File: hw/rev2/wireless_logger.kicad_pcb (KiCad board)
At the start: 4 copper layers, 98 parts, among them J1 FCI 10118194, J3 SSD1306_SER, J4 SWD_10PIN, Q1 2N7002P, Q2 2N7002P, U1 MT29FXX01A, U10 CC2541, U11 STM32F40X_BGA176, U2 MAG3110, U3 MMA8452Q, U4 LPS331AP, U5 L3GD20, U6 MCP111T-315, U7 BQ24095, U8 TPS62698, U9 CC1101, X1 FA-128 26.0000MF10Z-W3, X2 9HT10-32.768KBZF-T, X3 FA-128 32.0000MF20X-K3, X4 XRCGB25M000F0L00R0, X5 9HT10-32.768KBZF-T

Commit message: Uhhhh, secondary interconnect assignment and a LOT of routing
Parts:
- added C10: 100n, SMD0603, F.Cu at (195.9, 111.4)
- added C11: 100n, SMD0603, F.Cu at (198.6, 112.4)
- added C12: 100n, SMD0603, F.Cu at (182.8, 121.7)
- added C13: 10n, SMD0402, B.Cu at (179.1, 118.9)
- added C14: 2.2u, SMD0603, F.Cu at (184.4, 128.5)
- added C15: 100n, SMD0603, B.Cu at (177.0, 125.7)
- added C16: 100p, SMD0402, B.Cu at (186.2, 122.8)
- added C17: 100n, SMD0603, B.Cu at (177.4, 117.8)
- added C18: 1u, SMD0603, B.Cu at (176.4, 119.8)
- added C19: 10n, SMD0402, F.Cu at (176.2, 123.6)
- added C20: 2.2u, SMD0603, B.Cu at (187.4, 155.9)
- added C21: 2.2u, SMD0603, F.Cu at (191.9, 153.6)
- added C22: 10u, SMD0805, B.Cu at (198.5, 157.3)
- added C27: 1u, SMD0603, F.Cu at (173.5, 142.9)
- added C28: 15p, SMD0402, F.Cu at (170.6, 139.0)
- added C29: 15p, SMD0402, F.Cu at (170.6, 137.1)
- added C3: 2.2u, SMD0603, F.Cu at (190.8, 111.2)
- added C30: 1n, SMD0402, F.Cu at (181.6, 136.6)
- added C31: 12p, SMD0402, F.Cu at (178.8, 134.6)
- added C32: 12p, SMD0402, F.Cu at (182.5, 134.1)
- added C4: 100n, SMD0603, F.Cu at (182.7, 120.5)
- added C5: 100n, SMD0603, F.Cu at (197.4, 113.3)
- added C6: 100p, SMD0402, F.Cu at (183.3, 128.4)
- added C61: 10n, SMD0402, B.Cu at (172.2, 114.4)
- added C62: 10n, SMD0402, B.Cu at (172.9, 120.6)
- added C63: 10n, SMD0402, B.Cu at (172.7, 126.8)
- added C64: 10n, SMD0402, B.Cu at (173.1, 148.7)
- added C7: 1u, SMD0603, F.Cu at (193.3, 115.0)
- added C8: 100n, SMD0603, F.Cu at (180.0, 131.5)
- added C9: 100n, SMD0603, F.Cu at (190.9, 113.2)
- added J2: CONN_2, HDR_2X1_50MIL, F.Cu at (193.9, 158.7)
- added J5: CONN_5, HDR_5X1_50MIL, F.Cu at (184.5, 152.7)
- added P1: CONN_6X2, HDR_6X2_50MIL, F.Cu at (192.3, 128.3)
- added R30: 470k, SMD0402, B.Cu at (173.0, 112.1)
- added R31: 470k, SMD0402, B.Cu at (172.9, 117.5)
- added R32: 470k, SMD0402, B.Cu at (171.8, 126.8)
- added R33: 470k, SMD0402, B.Cu at (173.0, 146.6)
- added R34: 10k, SMD0402, B.Cu at (190.2, 126.3)
- added R35: 10k, SMD0402, B.Cu at (190.2, 127.5)
- C1, C26, C34, C35, C48, C54, C58, R10, R14, R16, R17, R18, R20, R21, R22, R5, R8, U1: moved to B.Cu
- C38: moved to F.Cu
- moved R12 43.6 mm to (196.6, 158.5)
- moved R25 43.5 mm to (193.1, 111.2)
- moved R26 42.1 mm to (192.9, 113.1), turned to 90 degrees
- moved R9 40.8 mm to (196.7, 151.7)
- moved R10 39.0 mm to (192.3, 157.0)
- moved R8 38.4 mm to (192.1, 156.0)
- moved R27 37.5 mm to (195.5, 131.4), turned to 180 degrees
- moved R28 37.3 mm to (195.5, 132.6), turned to 180 degrees
- moved R21 36.6 mm to (181.1, 110.7), turned to 180 degrees
- moved R11 36.2 mm to (191.9, 151.4), turned to 45 degrees
- moved C26 36.1 mm to (173.9, 158.2), turned to 180 degrees
- moved R13 35.9 mm to (178.5, 151.4), turned to 180 degrees
- moved R22 30.2 mm to (188.7, 138.1)
- moved R4 29.9 mm to (181.9, 125.3), turned to 180 degrees
- moved C54 29.8 mm to (188.1, 140.3)
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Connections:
- net N-00000242 renamed /Bluetooth/BT_ANT_DN
- net N-00000243 renamed /Bluetooth/BT_ANT_DP
- net N-00000244 renamed /Bluetooth/BT_ANT_SE
- C1 pad 2: VDD -> V3
- C2 pad 2: VDD -> V3
- C38 pad 2: N-0000078 -> V3
- C45 pad 2: VDD -> V3
- C46 pad 2: VDD -> V3
- C47 pad 2: VDD -> V3
- C48 pad 2: VDD -> V3
- C49 pad 2: VDD -> V3
- C50 pad 2: VDD -> V3
- C51 pad 2: VDD -> V3
- C52 pad 2: VDD -> V3
- C53 pad 2: VDD -> V3
- C54 pad 2: VDD -> V3
- C55 pad 2: VDD -> V3
- C56 pad 2: VDD -> V3
- C57 pad 2: VDD -> V3
- C58 pad 2: VDD -> V3
- D1 pad 1: VDD -> V3
- J3 pad 10: (no net) -> /STM32F4/OLED_nD/C
- J3 pad 7: VDD -> V3
- J3 pad 8: (no net) -> /STM32F4/OLED_nCS
- J4 pad 1: N-0000078 -> V3
- PB1 pad 1: /STM32F4/EXTI5 -> N-0000047
- PB2 pad 1: /STM32F4/EXTI6 -> N-0000046
- PB3 pad 1: /STM32F4/EXTI7 -> N-0000045
- PB4 pad 1: /STM32F4/EXTI8 -> N-0000044
- R13 pad 1: VDD -> V3
- R15 pad 2: VDD -> V3
- R16 pad 1: /STM32F4/BT_NRESET -> /Bluetooth/RF_RESET_N_LOCAL
- R17 pad 1: /STM32F4/BT_NRESET -> /Bluetooth/RF_RESET_N_LOCAL
- R20 pad 1: GND -> /OLED/OLED_GND
- R23 pad 1: VDD -> V3
- R24 pad 1: VDD -> V3
- R25 pad 1: VDD -> V3
- R26 pad 1: VDD -> V3
- R27 pad 2: (no net) -> /STM32F4/LED1
- R28 pad 2: (no net) -> /STM32F4/LED2
- R29 pad 2: (no net) -> /STM32F4/LED3
- R5 pad 1: VDD -> V3
- R6 pad 2: VDD -> V3
- R7 pad 2: VDD -> V3
- U1 pad D3: VDD -> V3
- U1 pad G5: VDD -> V3
- U1 pad G6: VDD -> V3
- U1 pad J8: VDD -> V3
- U1 pad K7: (no net) -> /STM32F4/FLASH_nCS
- U10 pad 10: VDD -> V3
- U10 pad 13: (no net) -> /STM32F4/EXTI2
- U10 pad 20: /STM32F4/BT_NRESET -> /Bluetooth/RF_RESET_N_LOCAL
- U10 pad 21: VDD -> V3
- U10 pad 24: VDD -> V3
- U10 pad 27: VDD -> V3
- U10 pad 28: VDD -> V3
- U10 pad 29: VDD -> V3
- U10 pad 31: VDD -> V3
- U10 pad 39: VDD -> V3
- U10 pad GND: (no net) -> GND
- U11 pad A1: (no net) -> /STM32F4/LED2
- U11 pad A2: (no net) -> /STM32F4/LED3
- U11 pad A4: (no net) -> /Sensors/ACC_INT1
- U11 pad A6: (no net) -> /STM32F4/GYRO_nCS
- U11 pad B1: (no net) -> /OLED/EN
- U11 pad B11: (no net) -> /STM32F4/UART2_RX
- U11 pad B2: (no net) -> /STM32F4/LED1
- U11 pad B5: (no net) -> /STM32F4/FLASH_nCS
- U11 pad B7: (no net) -> /Sensors/PRS_SPI_nCS
- U11 pad C11: (no net) -> /STM32F4/UART2_TX
- U11 pad C5: VDD -> V3
- U11 pad C6: VDD -> V3
- U11 pad C7: VDD -> V3
- U11 pad C8: VDD -> V3
- U11 pad C9: VDD -> V3
- U11 pad D1: (no net) -> /STM32F4/OLED_nCS
- U11 pad D2: (no net) -> /STM32F4/OLED_nRES
- U11 pad F14: (no net) -> /STM32F4/I2C3_SDA
- U11 pad F15: (no net) -> /STM32F4/I2C3_SCL
- U11 pad F3: VDD -> V3
- U11 pad G13: VDD -> V3
- U11 pad G14: (no net) -> /STM32F4/REG_nUSB_CONN
- U11 pad G15: (no net) -> /STM32F4/REG_nCHG
- U11 pad G3: VDD -> V3
- U11 pad H13: VDD -> V3
- U11 pad H15: (no net) -> /Power/MODE
- U11 pad J12: VDD -> V3
- U11 pad J13: VDD -> V3
- U11 pad K1: (no net) -> /STM32F4/EXTI7
- U11 pad K4: VDD -> V3
- U11 pad M3: (no net) -> /STM32F4/EXTI1
- U11 pad M6: (no net) -> /STM32F4/EXTI2
- U11 pad N10: VDD -> V3
- U11 pad N8: VDD -> V3
- U11 pad N9: VDD -> V3
- U11 pad P1: VDD -> V3
- U11 pad P12: (no net) -> /STM32F4/SPI2_NSS
- U11 pad R1: VDD -> V3
- U11 pad R10: (no net) -> /STM32F4/BT_NRESET
- U11 pad R11: (no net) -> /STM32F4/CC1101_nCS
- U11 pad R15: (no net) -> /STM32F4/SPI2_MOSI
- U11 pad R2: (no net) -> /STM32F4/OLED_nD/C
- U11 pad R8: /STM32F4/EXTI7 -> (no net)
- U2 pad 2: VDD -> V3
- U2 pad 8: VDD -> V3
- U3 pad 1: VDD -> V3
- U3 pad 11: (no net) -> /Sensors/ACC_INT1
- U3 pad 14: VDD -> V3
- U4 pad 1: VDD -> V3
- U4 pad 14: VDD -> V3
- U5 pad 1: VDD -> V3
- U5 pad 15: VDD -> V3
- U5 pad 16: VDD -> V3
- U7 pad 5: (no net) -> /STM32F4/REG_nUSB_CONN
- U7 pad 8: (no net) -> /STM32F4/REG_nCHG
- U7 pad GND: (no net) -> GND
- U8 pad 3: (no net) -> GND
- U9 pad 11: VDD -> V3
- U9 pad 18: VDD -> V3
- U9 pad 4: VDD -> V3
- U9 pad 9: VDD -> V3
- X1 pad GND: (no net) -> GND
- X3 pad GND: (no net) -> GND
- X4 pad GND: (no net) -> GND
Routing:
- net V3: track 0.00 -> 273.7 mm, vias 0 -> 27
- net GND: track 46.1 -> 245.8 mm, vias 2 -> 45
- net Vbat: track 0.00 -> 92.0 mm, vias 0 -> 8
- net /Sensors/GYR_SPI_MOSI: track 0.00 -> 82.8 mm, vias 0 -> 8
- net /OLED/SDIN: track 0.00 -> 68.9 mm, vias 0 -> 5
- net /Sensors/ACC_I2C_SCL: track 0.00 -> 66.0 mm, vias 0 -> 3
- net /OLED/SCLK: track 0.00 -> 64.7 mm, vias 0 -> 3
- net /Sensors/GYR_SPI_MISO: track 0.00 -> 59.5 mm, vias 0 -> 5
- net /STM32F4/I2C3_SDA: track 0.00 -> 56.6 mm, vias 0 -> 4
- net /Sensors/GYR_SPI_CLK: track 0.00 -> 56.4 mm, vias 0 -> 6
- net /STM32F4/I2C3_SCL: track 0.00 -> 55.9 mm, vias 0 -> 4
- net /Sensors/ACC_I2C_SDA: track 0.00 -> 53.2 mm, vias 0 -> 3
- net Vbus: track 0.00 -> 50.8 mm, vias 0 -> 2
- net /STM32F4/SPI2_CLK: track 0.00 -> 49.3 mm, vias 0 -> 3
- net /STM32F4/SPI2_NSS: track 0.00 -> 48.6 mm, vias 0 -> 3
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- added copper zone on GND_PLANE, net /OLED/OLED_GND
- added copper zone on B.Cu, net GND
- added copper zone on GND_PLANE, net GND
- added copper zone on Inner2.Cu, net V3
- removed copper zone on GND, net /OLED/OLED_GND
- removed copper zone on GND, net GND
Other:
- net class 50OHM added: clearance 0.1524, trace_width 0.2032, via_dia 0.635, via_drill 0.3048
- net class Default: trace_width 0.2032 -> 0.1524

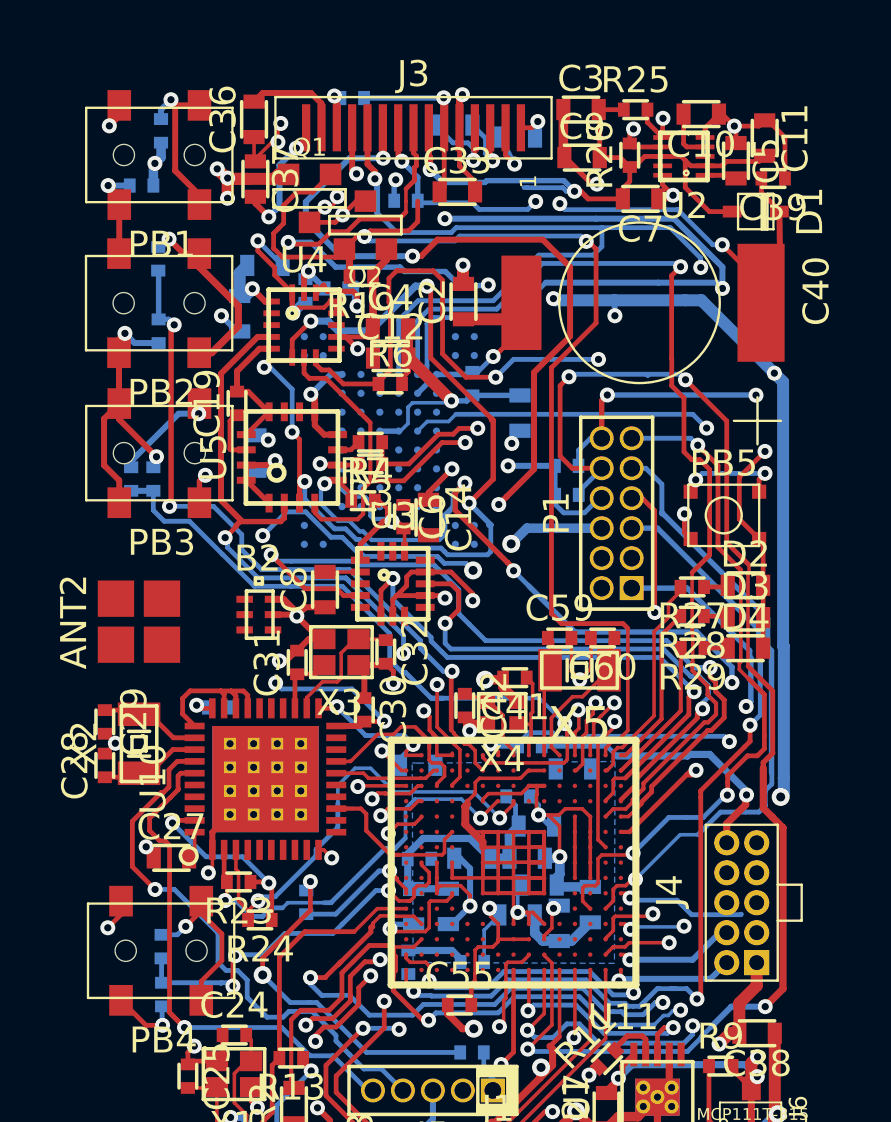
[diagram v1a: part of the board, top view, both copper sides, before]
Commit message: Optimized some routes and passes DRC. Still need to do RF traces
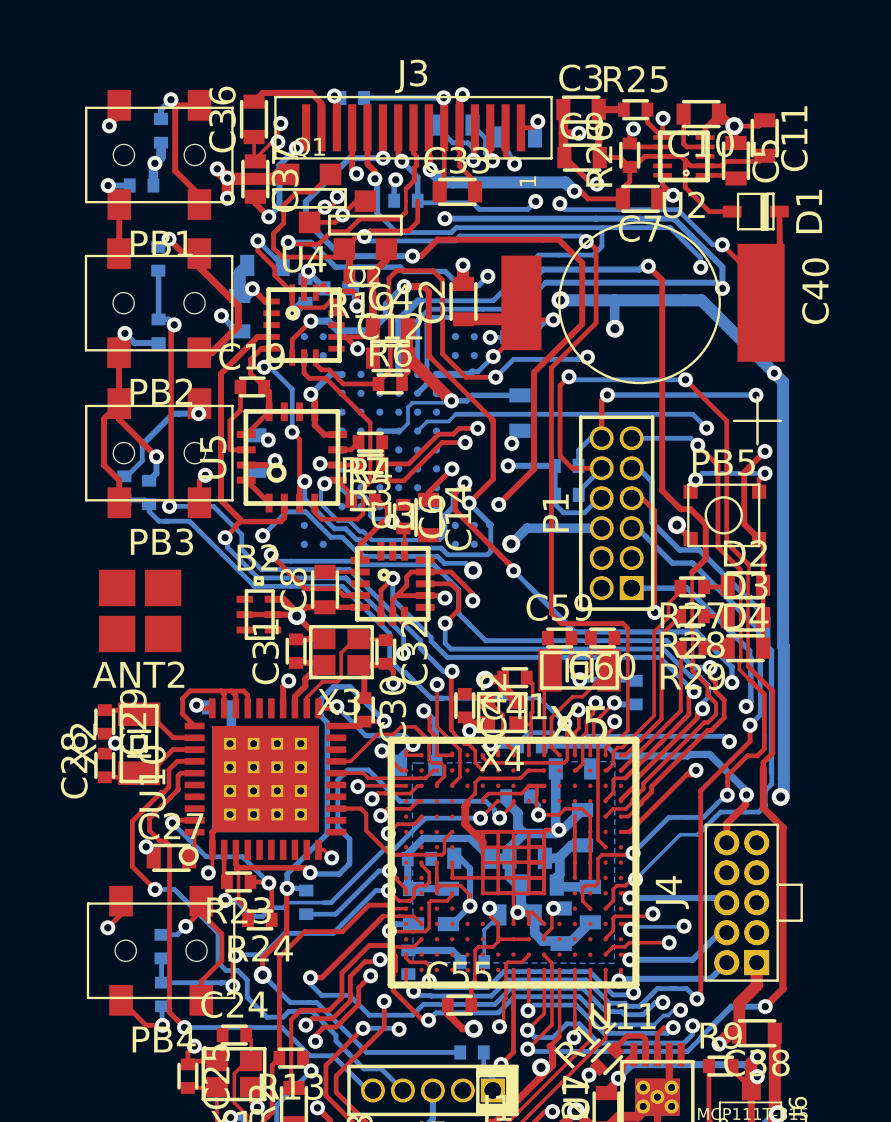
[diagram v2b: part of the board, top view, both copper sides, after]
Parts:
- C39: moved to B.Cu
- moved C39 22.6 mm to (193.1, 135.9), turned to 270 degrees
- moved C16 2.75 mm to (188.1, 120.8), turned to 180 degrees
- moved C49 1.96 mm to (190.9, 141.6), turned to 270 degrees
- moved C19 0.95 mm to (176.9, 122.9), turned to 0 degrees
- moved C63 0.60 mm to (172.5, 127.4)
- moved R32 0.48 mm to (171.5, 127.2)
- moved C31 0.48 mm to (178.7, 134.1)
- moved ANT2 0.46 mm to (172.1, 132.4), turned to 180 degrees
- moved C43 0.15 mm to (190.0, 145.8)
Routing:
- net GND: track 245.8 -> 266.7 mm, vias 45 -> 47
- net /STM32F4/GYRO_nCS: track 44.7 -> 36.9 mm
- net V3: track 273.7 -> 277.3 mm, vias 27 -> 28
- net /STM32F4/I2C2_SCL: track 19.8 -> 21.7 mm
- net /STM32F4/I2C2_SDA: track 18.9 -> 17.5 mm
- net N-00000182: track 2.30 -> 3.52 mm
- net /STM32F4/FLASH_nCS: track 41.9 -> 40.7 mm
- net /OLED/SCLK: track 64.7 -> 65.9 mm
- net N-0000065: track 5.12 -> 6.25 mm
- net /Bluetooth/RF_RESET_N_LOCAL: track 32.7 -> 31.7 mm, vias 4 -> 3
- net N-00000221: track 2.79 -> 3.71 mm
- net /STM32F4/SWO: track 5.49 -> 4.65 mm
- net /STM32F4/OLED_nD/C: track 45.2 -> 46.0 mm
- net N-0000067: track 47.7 -> 46.9 mm
- net N-0000045: track 8.87 -> 9.58 mm
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
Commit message: Ready for first schematic review
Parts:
- added C65: CAP, SMD0402, F.Cu at (173.7, 130.3)
- added C66: CAP, SMD0402, F.Cu at (171.9, 129.8)
- added PAD_0_5x1_5: VAL**, PAD_0_5x1_5, F.Cu at (170.9, 159.2)
- C28, C29, R15, X2: moved to B.Cu
- C61, C62, C63, C64: value 10n -> 100n
- R30, R31, R32, R33: value 470k -> 3.3k
- moved C29 4.67 mm to (175.0, 135.4), turned to 0 degrees
- moved C28 2.57 mm to (173.0, 139.9), turned to 180 degrees
- moved R13 2.44 mm to (177.1, 149.4), turned to 0 degrees
- moved ANT2 1.41 mm to (173.2, 133.4), turned to 270 degrees
- moved X2 1.12 mm to (173.0, 137.4)
- moved B2 0.93 mm to (176.8, 131.7)
- moved R9 0.81 mm to (196.6, 152.5)
- moved R15 0.80 mm to (173.8, 158.8)
- moved C26 0.79 mm to (174.6, 157.9)
- moved R14 0.23 mm to (176.3, 158.9), turned to 270 degrees
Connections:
- B2 pad 1: /Bluetooth/BT_ANT_SE -> N-00000226
- R33 pad 2: /STM32F4/EXTI8 -> (no net)
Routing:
- net V3: track 277.3 -> 306.4 mm, vias 28 -> 29
- net GND: track 266.7 -> 284.0 mm, vias 47 -> 59
- net /Bluetooth/BT_ANT_SE: track 0.00 -> 6.09 mm
- net /Bluetooth/BT_ANT_DP: track 0.00 -> 4.59 mm
- net /Bluetooth/BT_ANT_DN: track 0.00 -> 4.59 mm
- net /STM32F4/I2C3_SCL: track 55.9 -> 51.9 mm
- net Vbus: track 50.8 -> 54.1 mm, vias 2 -> 3
- net /STM32F4/REG_nUSB_CONN: track 19.6 -> 16.5 mm
- net N-00000194: track 0.00 -> 2.44 mm
- net N-00000226: track 0.00 -> 2.36 mm
- net N-00000199: track 0.00 -> 1.54 mm
- net Vbat: track 92.3 -> 90.8 mm, vias 8 -> 7
- net N-00000216: track 4.29 -> 3.32 mm, vias 0 -> 1
- net N-00000189: track 9.87 -> 9.13 mm
- net /STM32F4/EXTI8: track 16.5 -> 15.8 mm
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- added copper zone on F.Cu, net GND

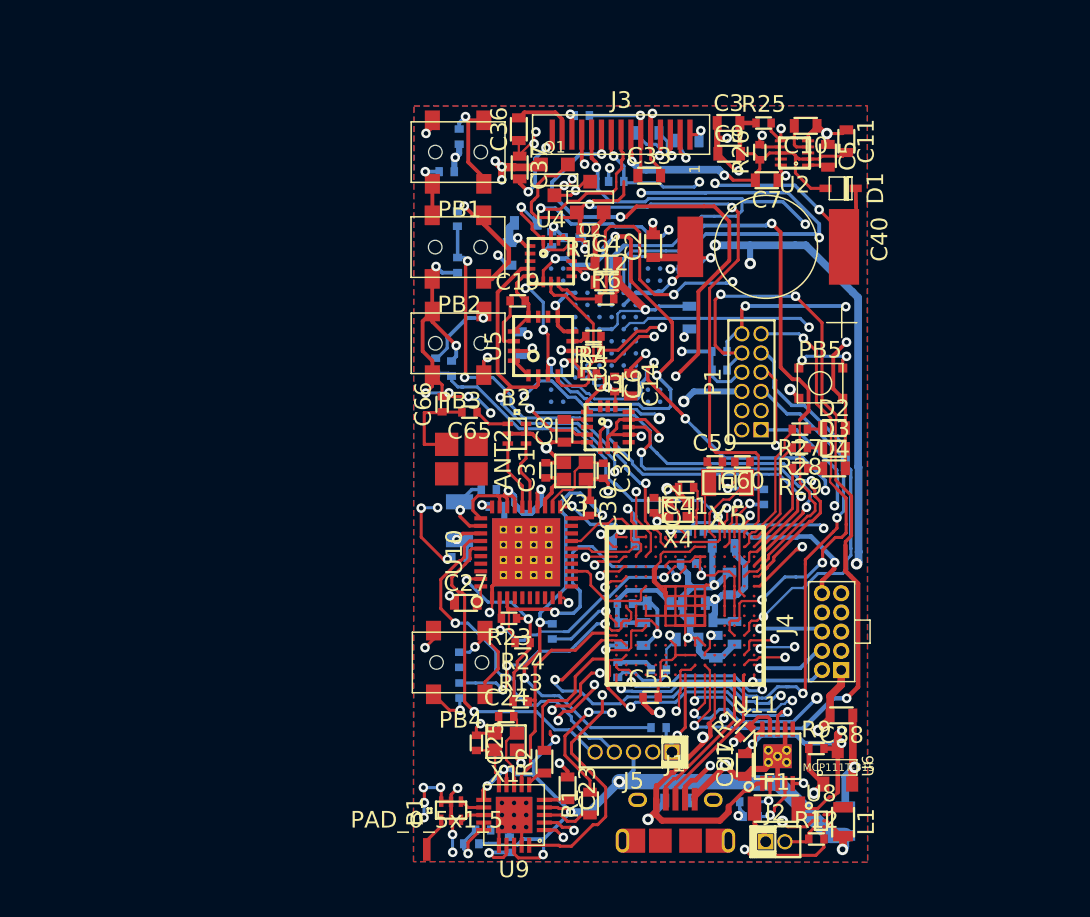
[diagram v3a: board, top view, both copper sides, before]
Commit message: Route and placement optimization. Added holes. Reduced number of ports used
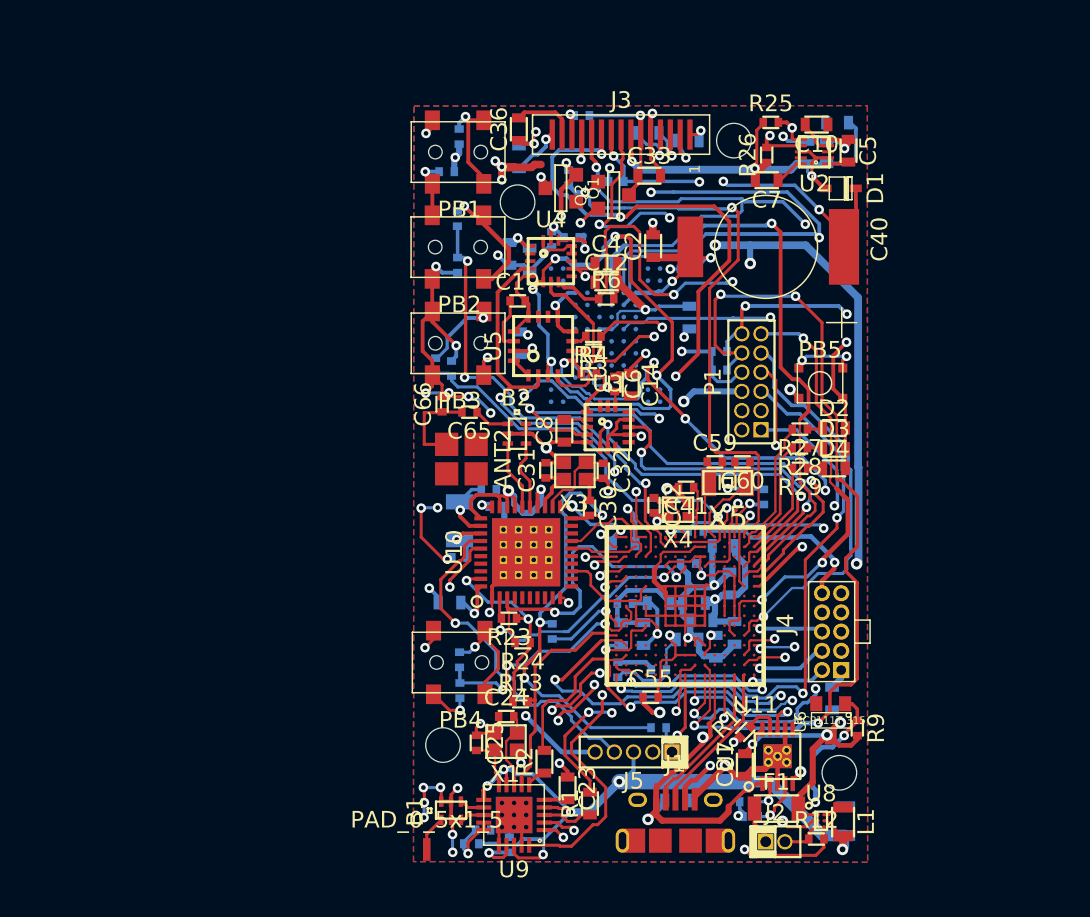
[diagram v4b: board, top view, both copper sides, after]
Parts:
- added SCREW_HOLE_2-56: VAL**, SCREW_HOLE_2-56, F.Cu at (172.0, 152.3)
- added SCREW_HOLE_2-56: VAL**, SCREW_HOLE_2-56, F.Cu at (191.2, 112.3)
- added SCREW_HOLE_2-56: VAL**, SCREW_HOLE_2-56, F.Cu at (198.1, 154.1)
- added SCREW_HOLE_2-56: VAL**, SCREW_HOLE_2-56, F.Cu at (176.9, 116.4)
- C11, C27, C3, C37, C38, C9, R19: moved to B.Cu
- C33: value 1u -> 2.2u
- moved C9 6.43 mm to (197.3, 113.1), turned to 270 degrees
- moved C3 5.58 mm to (196.0, 113.1), turned to 270 degrees
- moved R19 3.68 mm to (180.3, 114.8), turned to 270 degrees
- moved U6 3.14 mm to (197.6, 150.6), turned to 180 degrees
- moved R9 3.02 mm to (199.3, 151.2), turned to 270 degrees
- moved C17 2.44 mm to (177.7, 120.2), turned to 90 degrees
- moved Q2 1.55 mm to (183.2, 115.9), turned to 90 degrees
- moved C5 1.40 mm to (198.7, 113.0)
- moved C11 1.37 mm to (198.0, 111.1), turned to 0 degrees
- moved U2 1.32 mm to (196.5, 113.1)
- moved C38 1.27 mm to (197.7, 149.2), turned to 90 degrees
- moved C27 1.08 mm to (172.4, 142.9)
- moved C10 0.72 mm to (196.6, 111.3)
- moved Q1 0.69 mm to (179.7, 115.5), turned to 270 degrees
- moved C37 0.68 mm to (177.0, 113.4)
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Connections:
- B1 pad 1: N-00000194 (its old number) -> /Guardian Interface/GUARDIAN_ANT_SE
- PAD_0_5x1_5 pad 1: N-00000194 (its old number) -> /Guardian Interface/GUARDIAN_ANT_SE
- R33 pad 2: (no net) -> /STM32F4/EXTI8
- U11 pad B6: (no net) -> /Sensors/PRS_SPI_nCS
- U11 pad B7: /Sensors/PRS_SPI_nCS -> (no net)
- U11 pad D2: /STM32F4/OLED_nRES -> (no net)
- U11 pad F4: (no net) -> /STM32F4/OLED_nRES
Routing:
- net GND: track 284.0 -> 255.1 mm, vias 59 -> 54
- net /OLED/EN: track 49.4 -> 39.9 mm
- net /STM32F4/OLED_nCS: track 41.9 -> 36.0 mm
- net N-00000193: track 9.13 -> 14.2 mm, vias 2 -> 3
- net (no net): track 0.02 -> 5.00 mm, vias 0 -> 3
- net V3: track 306.4 -> 311.1 mm, vias 29 -> 28
- net /Sensors/GYR_SPI_MISO: track 59.6 -> 63.3 mm
- net /STM32F4/GYRO_nCS: track 36.9 -> 39.8 mm
- net /Bluetooth/RF_RESET_N_LOCAL: track 31.7 -> 29.1 mm
- net /Bluetooth/RF_DD: track 22.6 -> 20.1 mm, vias 1 -> 2
- net N-00000194 (its old number): track 2.44 -> 0.00 mm
- net /Guardian Interface/GUARDIAN_ANT_SE: track 0.00 -> 2.44 mm
- net /OLED/OLED_GND: track 19.6 -> 17.4 mm, vias 7 -> 5
- net N-00000234: track 5.52 -> 3.41 mm, vias 2 -> 1
- net /STM32F4/OLED_nRES: track 37.4 -> 39.5 mm
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
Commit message: Updated BQ24095 to MSOP package (free samples) and verified connections
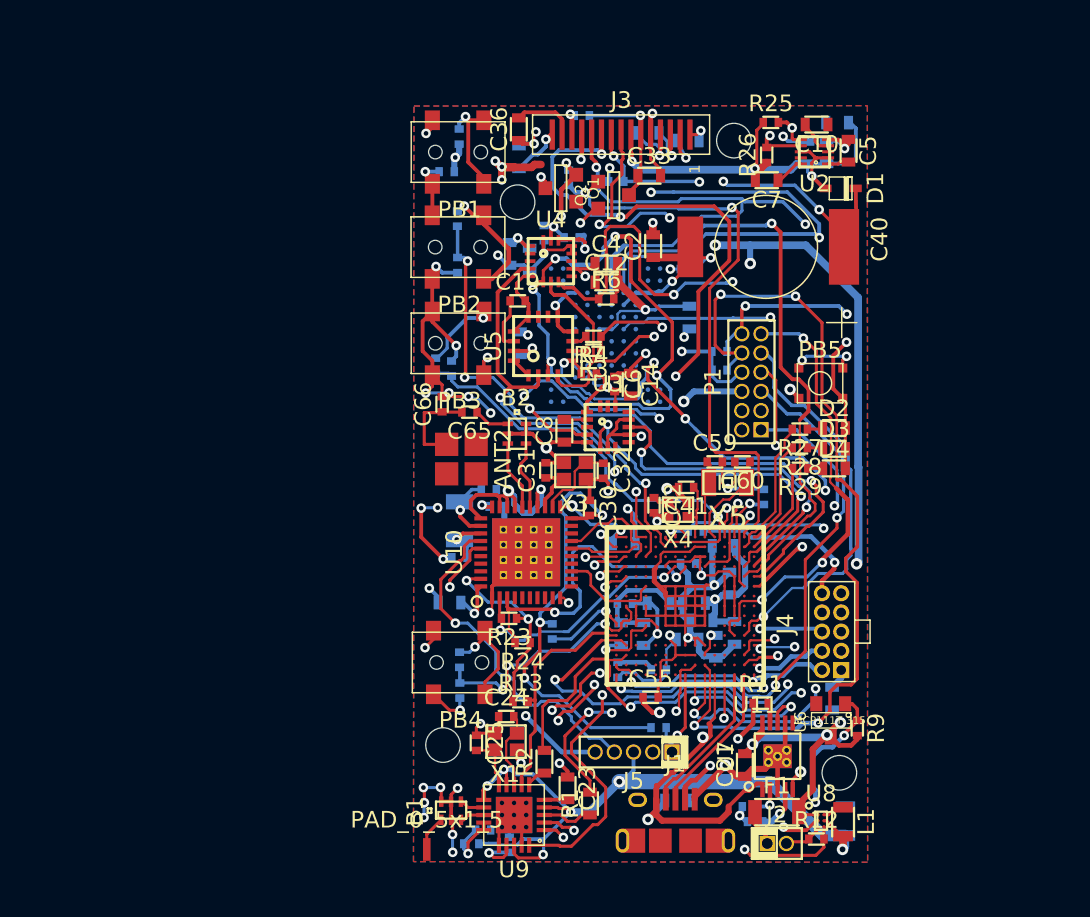
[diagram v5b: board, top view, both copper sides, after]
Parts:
- U7: footprint BQ24095 -> BQ24095_MSOP
- moved R11 2.15 mm to (192.9, 149.5), turned to 0 degrees
- moved C13 0.65 mm to (178.6, 118.4)
- moved R10 0.45 mm to (192.6, 157.3)
- moved R8 0.36 mm to (192.2, 156.3)
- moved F1 0.24 mm to (194.0, 156.7)
- moved J2 0.15 mm to (194.0, 158.8)
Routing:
- net /STM32F4/SPI2_NSS: track 48.1 -> 51.5 mm
- net GND: track 255.1 -> 257.7 mm
- net Vbat: track 88.9 -> 91.2 mm
- net /STM32F4/SPI2_MOSI: track 38.3 -> 36.6 mm
- net N-00000191: track 2.30 -> 1.36 mm
- net /STM32F4/SPI2_CLK: track 49.3 -> 49.9 mm
- net /STM32F4/REG_nCHG: track 10.2 -> 10.7 mm
